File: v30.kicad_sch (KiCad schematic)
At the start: 13 parts, among them U3 74ALVC164245, U4 74ALVC164245, U5 74ALVC164245

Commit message: Fab changes
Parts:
- C18: MPN C14663 -> C15849
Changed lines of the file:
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@@
 			)
 		)
-		(property "MPN" "C14663"
+		(property "MPN" "C15849"
 			(at 97.79 62.23 0)
 			(effects

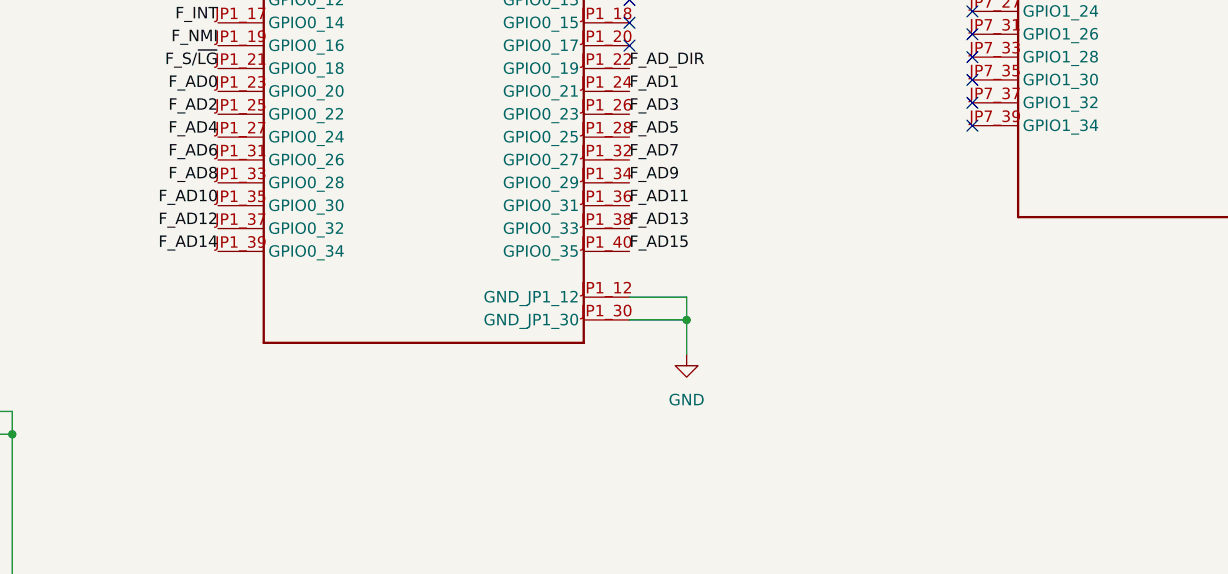
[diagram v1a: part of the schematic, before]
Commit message: Power tweaks. Revision 1 production submitted
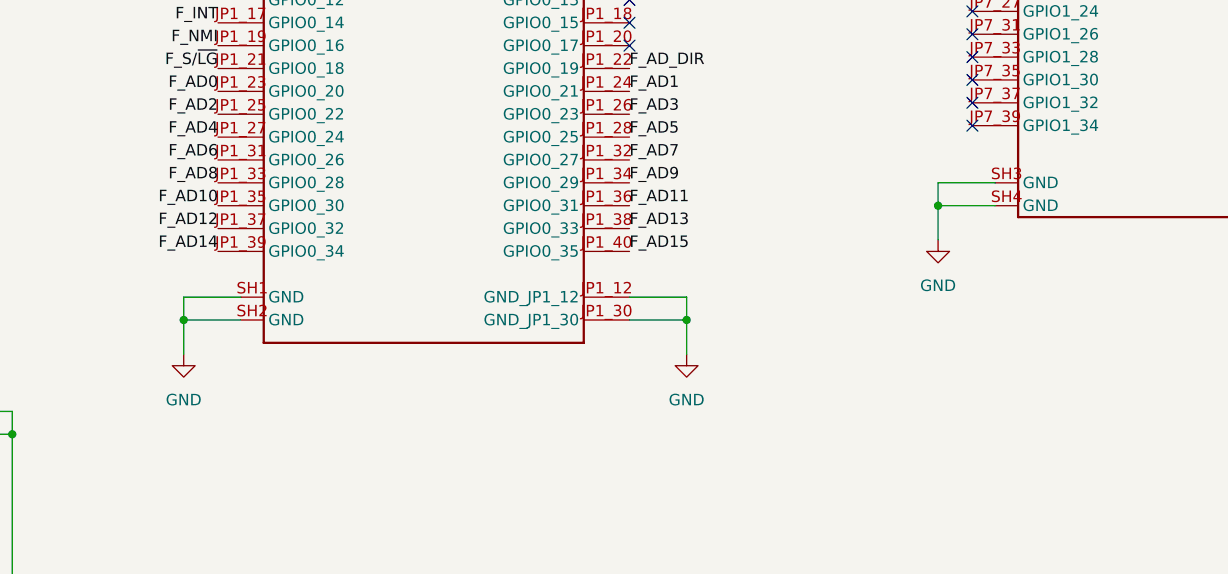
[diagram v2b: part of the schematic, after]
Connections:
- net GND: now also U2.SH1 (GND), U2.SH2 (GND), U2.SH3 (GND), U2.SH4 (GND)
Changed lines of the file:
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@@
 	)
 	(junction
+		(at 295.91 100.33)
+		(diameter 0)
+		(color 0 0 0 0)
+	)
+	(junction
 		(at 325.12 189.23)
 		(diameter 0)
@@
 	)
 	(junction
+		(at 212.09 113.03)
+		(diameter 0)
+		(color 0 0 0 0)
+	)
+	(junction
 		(at 377.19 189.23)
 		(diameter 0)
@@
 	(wire
 		(pts
+			(xy 212.09 113.03) (xy 212.09 116.84)
+		)
+		(stroke
+			(width 0)
+			(type default)
+		)
+	)
+	(wire
+		(pts
 			(xy 180.34 125.73) (xy 193.04 125.73)
 		)
@@
 	(wire
 		(pts
+			(xy 295.91 100.33) (xy 295.91 104.14)
+		)
+		(stroke
+			(width 0)
+			(type default)
+		)
+	)
+	(wire
+		(pts
 			(xy 325.12 204.47) (xy 325.12 207.01)
 		)
@@
 	(wire
 		(pts
+			(xy 302.26 100.33) (xy 295.91 100.33)
+		)
+		(stroke
+			(width 0)
+			(type default)
+		)
+	)
+	(wire
+		(pts
 			(xy 364.49 189.23) (xy 377.19 189.23)
 		)
@@
 	(wire
 		(pts
+			(xy 295.91 97.79) (xy 295.91 100.33)
+		)
+		(stroke
+			(width 0)
+			(type default)
+		)
+	)
+	(wire
+		(pts
 			(xy 351.79 99.06) (xy 351.79 102.87)
 		)
@@
 	(wire
 		(pts
+			(xy 218.44 113.03) (xy 212.09 113.03)
+		)
+		(stroke
+			(width 0)
+			(type default)
+		)
+	)
+	(wire
+		(pts
+			(xy 212.09 110.49) (xy 212.09 113.03)
+		)
+		(stroke
+			(width 0)
+			(type default)
+		)
+	)
+	(wire
+		(pts
 			(xy 339.09 173.99) (xy 336.55 173.99)
 		)
@@
 	(wire
 		(pts
+			(xy 302.26 97.79) (xy 295.91 97.79)
+		)
+		(stroke
+			(width 0)
+			(type default)
+		)
+	)
+	(wire
+		(pts
 			(xy 377.19 217.17) (xy 377.19 207.01)
 		)
@@
 	(wire
 		(pts
+			(xy 218.44 110.49) (xy 212.09 110.49)
+		)
+		(stroke
+			(width 0)
+			(type default)
+		)
+	)
+	(wire
+		(pts
 			(xy 364.49 207.01) (xy 377.19 207.01)
 		)
@@
 	)
 	(symbol
+		(lib_id "power:GND")
+		(at 295.91 104.14 0)
+		(mirror y)
+		(unit 1)
+		(exclude_from_sim no)
+		(in_bom yes)
+		(on_board yes)
+		(dnp no)
+		(fields_autoplaced yes)
+		(property "Reference" "#PWR015"
+			(at 295.91 110.49 0)
+			(effects
+				(font
+					(size 1.27 1.27)
+				)
+				(hide yes)
+			)
+		)
+		(property "Value" "GND"
+			(at 295.91 109.22 0)
+			(effects
+				(font
+					(size 1.27 1.27)
+				)
+			)
+		)
+		(property "Footprint" ""
+			(at 295.91 104.14 0)
+			(effects
+				(font
+					(size 1.27 1.27)
+				)
+				(hide yes)
+			)
+		)
+		(property "Datasheet" ""
+			(at 295.91 104.14 0)
+			(effects
+				(font
+					(size 1.27 1.27)
+				)
+				(hide yes)
+			)
+		)
+		(property "Description" "Power symbol creates a global label with name \"GND\" , ground"
+			(at 295.91 104.14 0)
+			(effects
+				(font
+					(size 1.27 1.27)
+				)
+				(hide yes)
+			)
+		)
+		(pin "1"
+		)
+		(instances
+			(project "NEC-DE10"
+				(path "/ddde7423-f6ec-43a3-9d7f-3b7e70f4bb41/3b286c9a-9872-4946-88af-68c784bc6794"
+					(reference "#PWR015")
+					(unit 1)
+				)
+			)
+		)
+	)
+	(symbol
 		(lib_id "74xx:74ALVC164245")
 		(at 153.67 227.33 0)
@@
 	)
 	(symbol
+		(lib_id "power:GND")
+		(at 212.09 116.84 0)
+		(mirror y)
+		(unit 1)
+		(exclude_from_sim no)
+		(in_bom yes)
+		(on_board yes)
+		(dnp no)
+		(fields_autoplaced yes)
+		(property "Reference" "#PWR013"
+			(at 212.09 123.19 0)
+			(effects
+				(font
+					(size 1.27 1.27)
+				)
+				(hide yes)
+			)
+		)
+		(property "Value" "GND"
+			(at 212.09 121.92 0)
+			(effects
+				(font
+					(size 1.27 1.27)
+				)
+			)
+		)
+		(property "Footprint" ""
+			(at 212.09 116.84 0)
+			(effects
+				(font
+					(size 1.27 1.27)
+				)
+				(hide yes)
+			)
+		)
+		(property "Datasheet" ""
+			(at 212.09 116.84 0)
+			(effects
+				(font
+					(size 1.27 1.27)
+				)
+				(hide yes)
+			)
+		)
+		(property "Description" "Power symbol creates a global label with name \"GND\" , ground"
+			(at 212.09 116.84 0)
+			(effects
+				(font
+					(size 1.27 1.27)
+				)
+				(hide yes)
+			)
+		)
+		(pin "1"
+		)
+		(instances
+			(project "NEC-DE10"
+				(path "/ddde7423-f6ec-43a3-9d7f-3b7e70f4bb41/3b286c9a-9872-4946-88af-68c784bc6794"
+					(reference "#PWR013")
+					(unit 1)
+				)
+			)
+		)
+	)
+	(symbol
 		(lib_id "NEC-DE10:P0496")
 		(at 322.58 71.12 0)
@@
 		(pin "JP1_17"
 		)
+		(pin "SH1"
+		)
+		(pin "SH2"
+		)
+		(pin "SH3"
+		)
+		(pin "SH4"
+		)
 		(instances
 			(project "NEC-DE10"
@@
 	)
 	(symbol
+		(lib_name "P0496_1")
 		(lib_id "NEC-DE10:P0496")
 		(at 238.76 82.55 0)
@@
 		(pin "JP1_17"
 		)
+		(pin "SH1"
+		)
+		(pin "SH2"
+		)
+		(pin "SH3"
+		)
+		(pin "SH4"
+		)
 		(instances

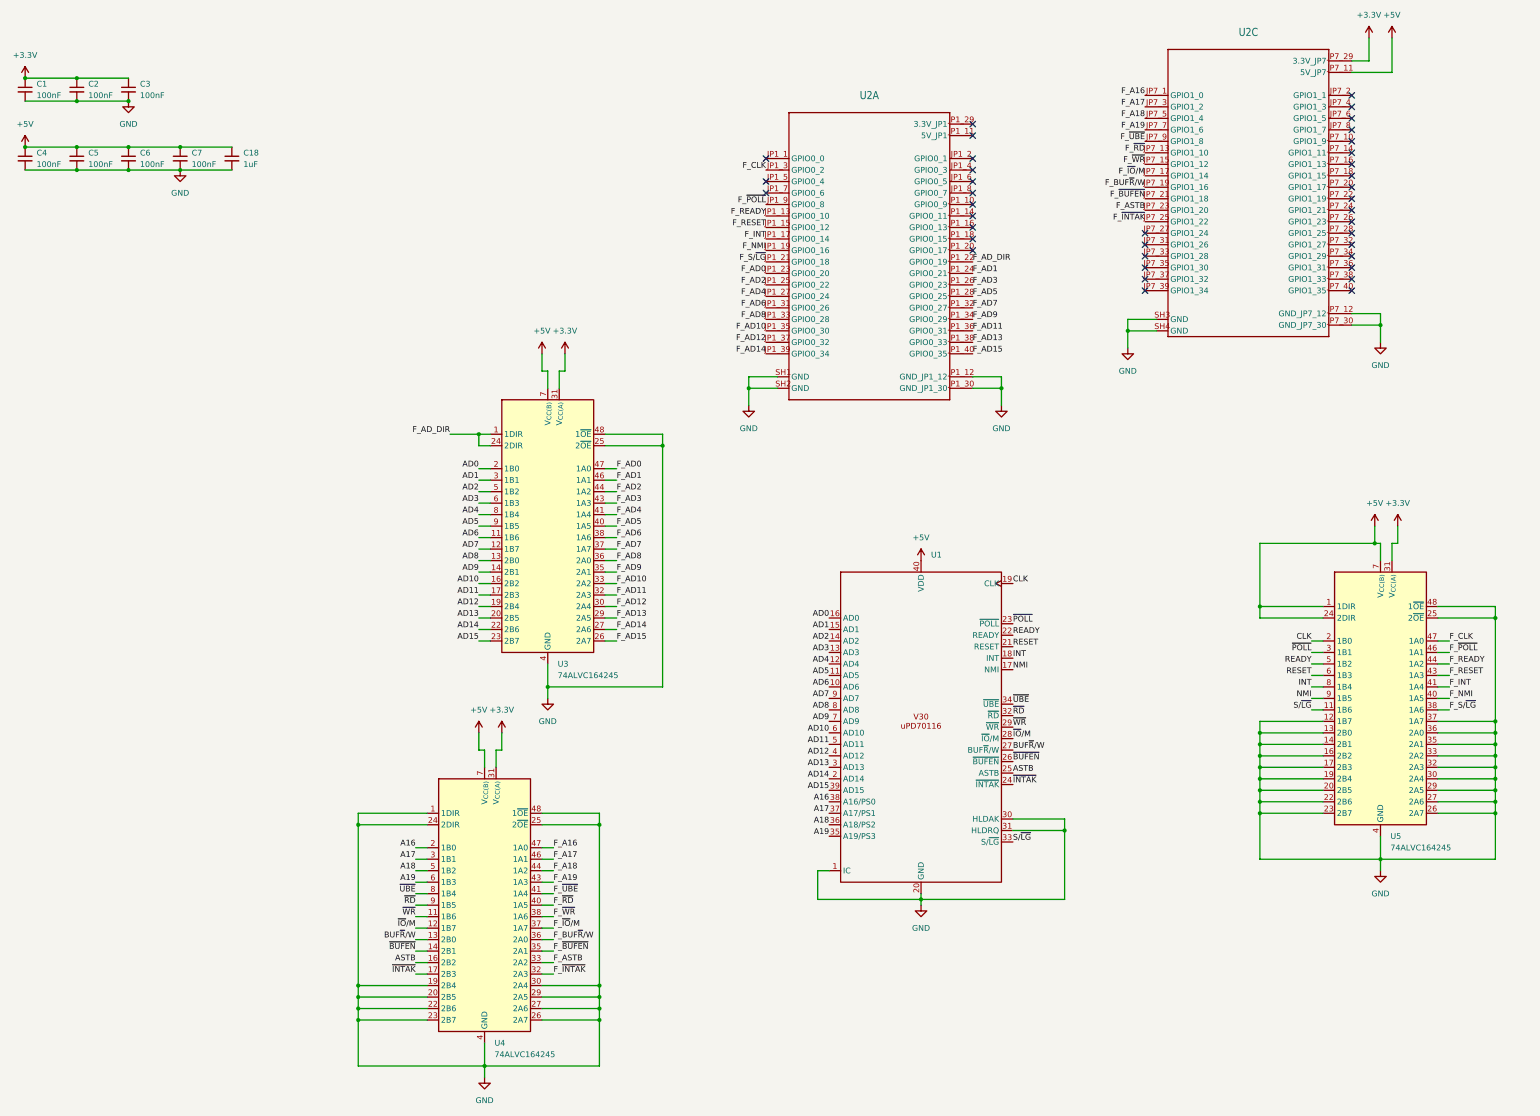
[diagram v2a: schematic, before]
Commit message: Adding power control Moving board around for heat issues
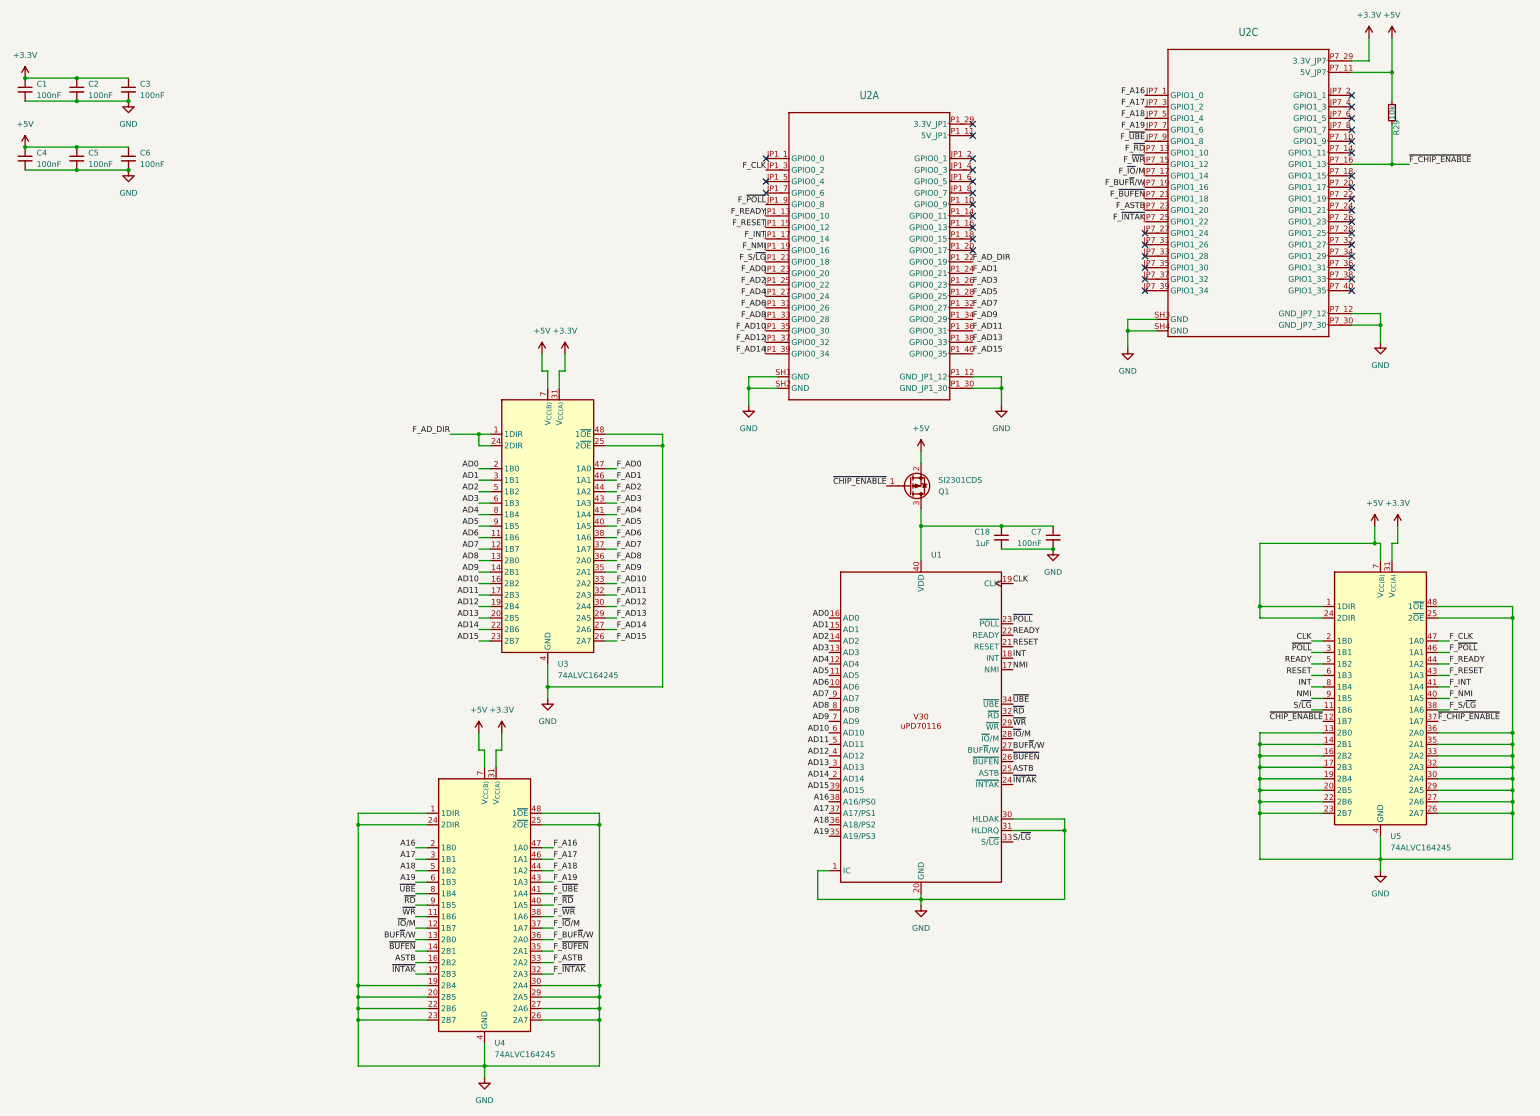
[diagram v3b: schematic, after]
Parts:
- added Q1: SI2301CDS, Package_TO_SOT_SMD:SOT-23, symbol Device:Q_PMOS_GSD
- added R29: 10k, Resistor_SMD:R_0603_1608Metric, symbol Device:R_Small
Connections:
- net +5V: now also Q1.2 (S), R29.2; no longer C18.1, C7.1, U1.40 (VDD)
- net GND: no longer U5.12 (1B7), U5.37 (1A7)
- net ~{F_CHIP_ENABLE}: now reaches U2.JP7_16 (GPIO1_13)
- net ~{F_CHIP_ENABLE}: now also U5.37 (1A7), R29.1
- new net: C18.1, C7.1, Q1.3 (D), U1.40 (VDD)
- new net ~{CHIP_ENABLE}: Q1.1 (G), U5.12 (1B7)
- no-connect marks 38 -> 37
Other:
- moved on the sheet: C18, C7
